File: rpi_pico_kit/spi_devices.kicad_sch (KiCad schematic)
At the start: 32 parts, among them J6 Conn_01x08_Male, J7 Conn_01x08_Male, J8 Conn_01x08_Male, J9 Micro_SD_Card_Det, SW10 SW_Push, SW7 SW_Push, SW8 SW_Push, SW9 SW_Push, U7 MCP23S08-xSO

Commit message: changed switches from tht to smd
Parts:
- SW10, SW7, SW8, SW9: footprint Button_Switch_THT:SW_TH_Tactile_Omron_B3F-10xx -> Button_Switch_SMD:SW_SPST_Omron_B3FS-100xP; Manufacturer Part Number LA215000 -> TD-03XAT-A00-TR; Supplier Laskakit -> GME; Supplier Part URL https://www.laskakit.cz/tlacitko-6x6x5mm/ -> https://www.gme.cz/td-03xa-t-smd
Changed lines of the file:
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@@
       (effects (font (size 1.27 1.27)) (justify right))
     )
-    (property "Footprint" "Button_Switch_THT:SW_TH_Tactile_Omron_B3F-10xx" (id 2) (at 128.27 38.1 0)
+    (property "Footprint" "Button_Switch_SMD:SW_SPST_Omron_B3FS-100xP" (id 2) (at 128.27 38.1 0)
       (effects (font (size 1.27 1.27)) hide)
     )
@@
       (effects (font (size 1.27 1.27)) hide)
     )
-    (property "Manufacturer Part Number" "LA215000" (id 4) (at 133.35 38.1 0)
-      (effects (font (size 1.27 1.27)) hide)
-    )
-    (property "Supplier" "Laskakit" (id 5) (at 133.35 38.1 0)
-      (effects (font (size 1.27 1.27)) hide)
-    )
-    (property "Supplier Part URL" "https://www.laskakit.cz/tlacitko-6x6x5mm/" (id 6) (at 133.35 38.1 0)
+    (property "Manufacturer Part Number" "TD-03XAT-A00-TR" (id 4) (at 133.35 38.1 0)
+      (effects (font (size 1.27 1.27)) hide)
+    )
+    (property "Supplier" "GME" (id 5) (at 133.35 38.1 0)
+      (effects (font (size 1.27 1.27)) hide)
+    )
+    (property "Supplier Part URL" "https://www.gme.cz/td-03xa-t-smd" (id 6) (at 133.35 38.1 0)
       (effects (font (size 1.27 1.27)) hide)
     )
@@
       (effects (font (size 1.27 1.27)) (justify right))
     )
-    (property "Footprint" "Button_Switch_THT:SW_TH_Tactile_Omron_B3F-10xx" (id 2) (at 166.37 38.1 0)
+    (property "Footprint" "Button_Switch_SMD:SW_SPST_Omron_B3FS-100xP" (id 2) (at 166.37 38.1 0)
       (effects (font (size 1.27 1.27)) hide)
     )
@@
       (effects (font (size 1.27 1.27)) hide)
     )
-    (property "Manufacturer Part Number" "LA215000" (id 4) (at 171.45 38.1 0)
-      (effects (font (size 1.27 1.27)) hide)
-    )
-    (property "Supplier" "Laskakit" (id 5) (at 171.45 38.1 0)
-      (effects (font (size 1.27 1.27)) hide)
-    )
-    (property "Supplier Part URL" "https://www.laskakit.cz/tlacitko-6x6x5mm/" (id 6) (at 171.45 38.1 0)
+    (property "Manufacturer Part Number" "TD-03XAT-A00-TR" (id 4) (at 171.45 38.1 0)
+      (effects (font (size 1.27 1.27)) hide)
+    )
+    (property "Supplier" "GME" (id 5) (at 171.45 38.1 0)
+      (effects (font (size 1.27 1.27)) hide)
+    )
+    (property "Supplier Part URL" "https://www.gme.cz/td-03xa-t-smd" (id 6) (at 171.45 38.1 0)
       (effects (font (size 1.27 1.27)) hide)
     )
@@
       (effects (font (size 1.27 1.27)) (justify right))
     )
-    (property "Footprint" "Button_Switch_THT:SW_TH_Tactile_Omron_B3F-10xx" (id 2) (at 140.97 38.1 0)
+    (property "Footprint" "Button_Switch_SMD:SW_SPST_Omron_B3FS-100xP" (id 2) (at 140.97 38.1 0)
       (effects (font (size 1.27 1.27)) hide)
     )
@@
       (effects (font (size 1.27 1.27)) hide)
     )
-    (property "Manufacturer Part Number" "LA215000" (id 4) (at 146.05 38.1 0)
-      (effects (font (size 1.27 1.27)) hide)
-    )
-    (property "Supplier" "Laskakit" (id 5) (at 146.05 38.1 0)
-      (effects (font (size 1.27 1.27)) hide)
-    )
-    (property "Supplier Part URL" "https://www.laskakit.cz/tlacitko-6x6x5mm/" (id 6) (at 146.05 38.1 0)
+    (property "Manufacturer Part Number" "TD-03XAT-A00-TR" (id 4) (at 146.05 38.1 0)
+      (effects (font (size 1.27 1.27)) hide)
+    )
+    (property "Supplier" "GME" (id 5) (at 146.05 38.1 0)
+      (effects (font (size 1.27 1.27)) hide)
+    )
+    (property "Supplier Part URL" "https://www.gme.cz/td-03xa-t-smd" (id 6) (at 146.05 38.1 0)
       (effects (font (size 1.27 1.27)) hide)
     )
@@
       (effects (font (size 1.27 1.27)) (justify right))
     )
-    (property "Footprint" "Button_Switch_THT:SW_TH_Tactile_Omron_B3F-10xx" (id 2) (at 153.67 38.1 0)
+    (property "Footprint" "Button_Switch_SMD:SW_SPST_Omron_B3FS-100xP" (id 2) (at 153.67 38.1 0)
       (effects (font (size 1.27 1.27)) hide)
     )
@@
       (effects (font (size 1.27 1.27)) hide)
     )
-    (property "Manufacturer Part Number" "LA215000" (id 4) (at 158.75 38.1 0)
-      (effects (font (size 1.27 1.27)) hide)
-    )
-    (property "Supplier" "Laskakit" (id 5) (at 158.75 38.1 0)
-      (effects (font (size 1.27 1.27)) hide)
-    )
-    (property "Supplier Part URL" "https://www.laskakit.cz/tlacitko-6x6x5mm/" (id 6) (at 158.75 38.1 0)
-      (effects (font (size 1.27 1.27)) hide)
-    )
+    (property "Manufacturer Part Number" "TD-03XAT-A00-TR" (id 4) (at 158.75 38.1 0)
+      (effects (font (size 1.27 1.27)) hide)
+    )
+    (property "Supplier" "GME" (id 5) (at 158.75 38.1 0)
+      (effects (font (size 1.27 1.27)) hide)
+    )
+    (property "Supplier Part URL" "https://www.gme.cz/td-03xa-t-smd" (id 6) (at 158.75 38.1 0)
+      (effects (font (size 1.27 1.27)) hide)
+    )

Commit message: changed footprint for tactile switches, added 3D model
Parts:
- SW10, SW7, SW8, SW9: footprint Button_Switch_SMD:SW_SPST_Omron_B3FS-100xP -> Button_Switch_SMD:SW_SPST_Omron_B3FS-100xP_12
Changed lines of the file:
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@@
       (effects (font (size 1.27 1.27)) (justify right))
     )
-    (property "Footprint" "Button_Switch_SMD:SW_SPST_Omron_B3FS-100xP" (id 2) (at 128.27 38.1 0)
+    (property "Footprint" "Button_Switch_SMD:SW_SPST_Omron_B3FS-100xP_12" (id 2) (at 128.27 38.1 0)
       (effects (font (size 1.27 1.27)) hide)
     )
@@
       (effects (font (size 1.27 1.27)) (justify right))
     )
-    (property "Footprint" "Button_Switch_SMD:SW_SPST_Omron_B3FS-100xP" (id 2) (at 166.37 38.1 0)
+    (property "Footprint" "Button_Switch_SMD:SW_SPST_Omron_B3FS-100xP_12" (id 2) (at 166.37 38.1 0)
       (effects (font (size 1.27 1.27)) hide)
     )
@@
       (effects (font (size 1.27 1.27)) (justify right))
     )
-    (property "Footprint" "Button_Switch_SMD:SW_SPST_Omron_B3FS-100xP" (id 2) (at 140.97 38.1 0)
+    (property "Footprint" "Button_Switch_SMD:SW_SPST_Omron_B3FS-100xP_12" (id 2) (at 140.97 38.1 0)
       (effects (font (size 1.27 1.27)) hide)
     )
@@
       (effects (font (size 1.27 1.27)) (justify right))
     )
-    (property "Footprint" "Button_Switch_SMD:SW_SPST_Omron_B3FS-100xP" (id 2) (at 153.67 38.1 0)
-      (effects (font (size 1.27 1.27)) hide)
-    )
+    (property "Footprint" "Button_Switch_SMD:SW_SPST_Omron_B3FS-100xP_12" (id 2) (at 153.67 38.1 0)
+      (effects (font (size 1.27 1.27)) hide)
+    )

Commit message: created Custom library with custom SMD button switch
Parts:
- SW10, SW7, SW8, SW9: footprint Button_Switch_SMD:SW_SPST_Omron_B3FS-100xP_12 -> Custom:SW_SPST_Omron_B3FS-100xP_12
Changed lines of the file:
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@@
       (effects (font (size 1.27 1.27)) (justify right))
     )
-    (property "Footprint" "Button_Switch_SMD:SW_SPST_Omron_B3FS-100xP_12" (id 2) (at 128.27 38.1 0)
+    (property "Footprint" "Custom:SW_SPST_Omron_B3FS-100xP_12" (id 2) (at 128.27 38.1 0)
       (effects (font (size 1.27 1.27)) hide)
     )
@@
       (effects (font (size 1.27 1.27)) (justify right))
     )
-    (property "Footprint" "Button_Switch_SMD:SW_SPST_Omron_B3FS-100xP_12" (id 2) (at 166.37 38.1 0)
+    (property "Footprint" "Custom:SW_SPST_Omron_B3FS-100xP_12" (id 2) (at 166.37 38.1 0)
       (effects (font (size 1.27 1.27)) hide)
     )
@@
       (effects (font (size 1.27 1.27)) (justify right))
     )
-    (property "Footprint" "Button_Switch_SMD:SW_SPST_Omron_B3FS-100xP_12" (id 2) (at 140.97 38.1 0)
+    (property "Footprint" "Custom:SW_SPST_Omron_B3FS-100xP_12" (id 2) (at 140.97 38.1 0)
       (effects (font (size 1.27 1.27)) hide)
     )
@@
       (effects (font (size 1.27 1.27)) (justify right))
     )
-    (property "Footprint" "Button_Switch_SMD:SW_SPST_Omron_B3FS-100xP_12" (id 2) (at 153.67 38.1 0)
-      (effects (font (size 1.27 1.27)) hide)
-    )
+    (property "Footprint" "Custom:SW_SPST_Omron_B3FS-100xP_12" (id 2) (at 153.67 38.1 0)
+      (effects (font (size 1.27 1.27)) hide)
+    )

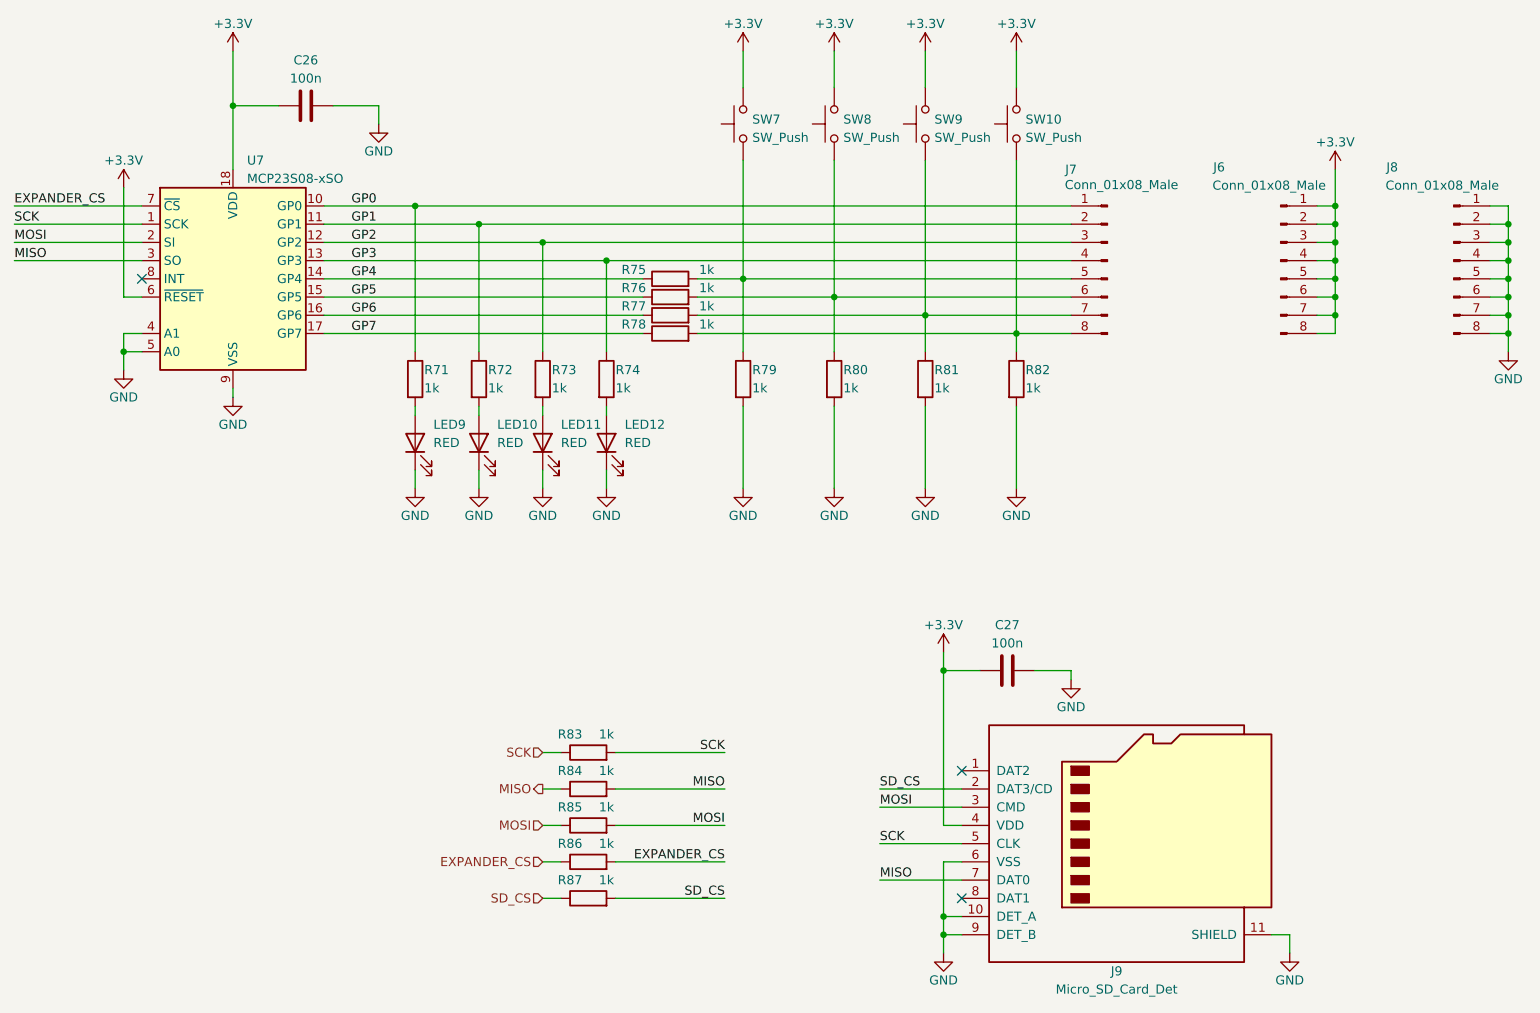
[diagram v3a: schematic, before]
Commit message: changed resistors to resistor arrays
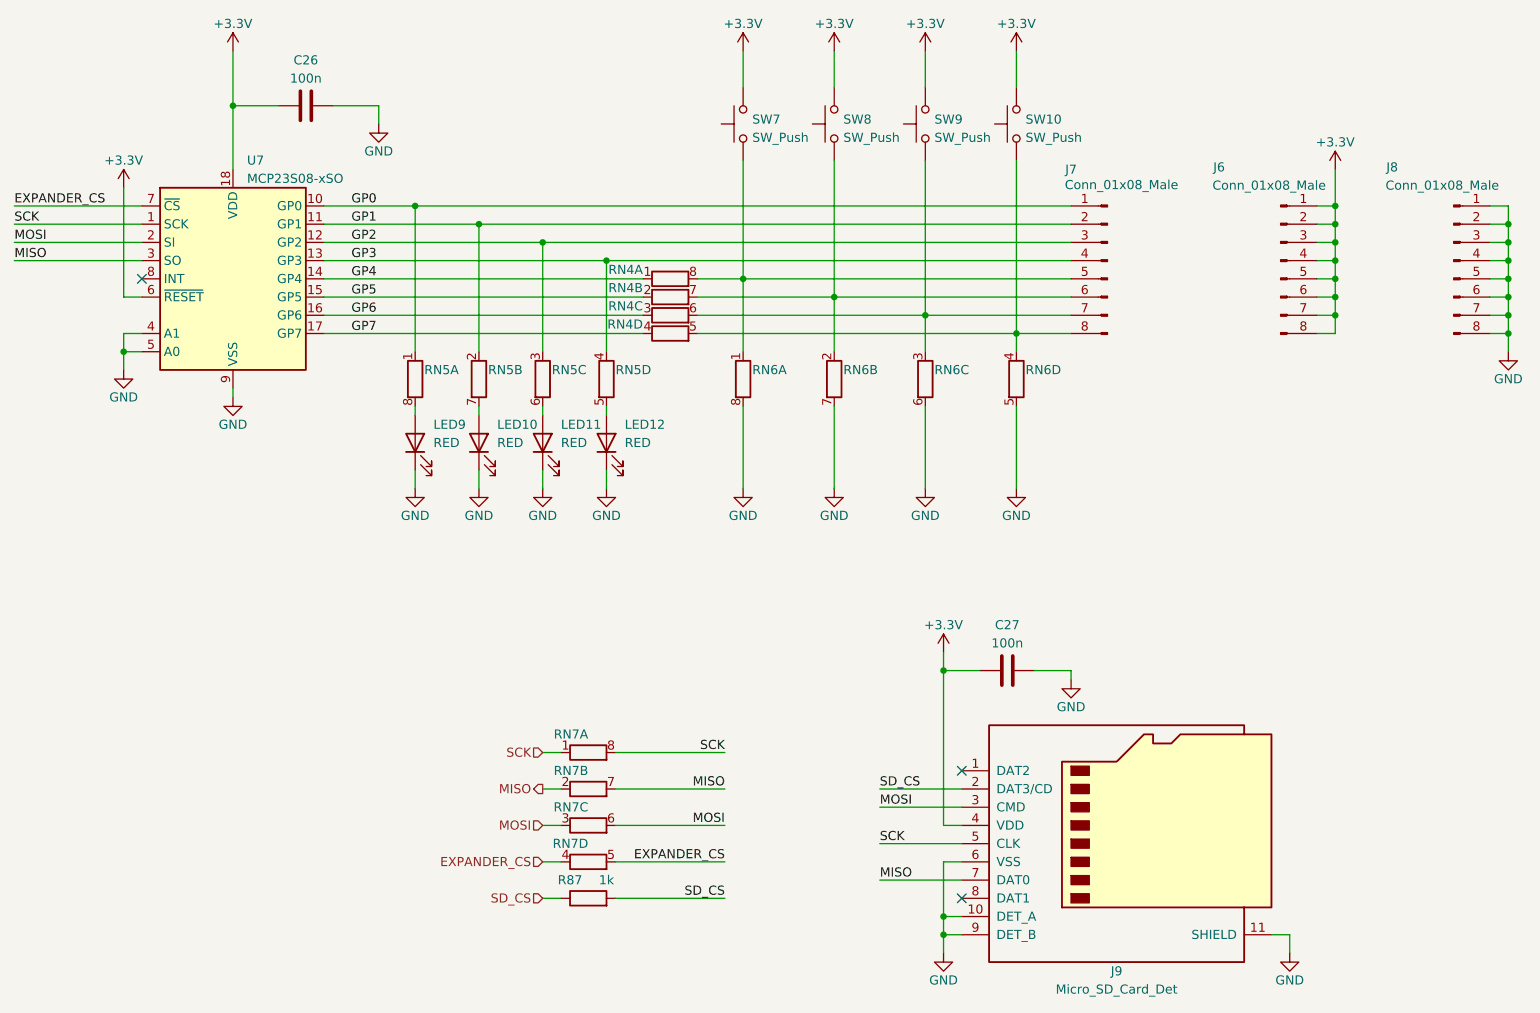
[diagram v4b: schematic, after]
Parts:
- removed R71, R72, R73, R74, R75, R76, R77, R78, R79, R80, R81, R82, R83, R84, R85, R86: 1k, Resistor_SMD:R_0805_2012Metric_Pad1.20x1.40mm_HandSolder, symbol Device:R
- added RN4, RN5, RN6, RN7: (no value), symbol Device:R_Pack04_Split
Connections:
- net EXPANDER_CS: now also RN7.4 (R4.1), RN7.5 (R4.2)
- net GND: now also RN6.5 (R4.2), RN6.6 (R3.2), RN6.7 (R2.2), RN6.8 (R1.2)
- net GP0: now also RN5.1 (R1.1)
- net GP1: now also RN5.2 (R2.1)
- net GP2: now also RN5.3 (R3.1)
- net GP3: now also RN5.4 (R4.1)
- net GP4: now also RN4.1 (R1.1)
- net GP5: now also RN4.2 (R2.1)
- net GP6: now also RN4.3 (R3.1)
- net GP7: now also RN4.4 (R4.1)
- net MISO: now also RN7.2 (R2.1), RN7.7 (R2.2)
- net MOSI: now also RN7.3 (R3.1), RN7.6 (R3.2)
- net SCK: now also RN7.1 (R1.1), RN7.8 (R1.2)
- net at LED10.2 (A): now also RN5.7 (R2.2)
- net at J7.6 (Pin_6), SW8.1: now also RN4.7 (R2.2), RN6.2 (R2.1)
- net at LED12.2 (A): now also RN5.5 (R4.2)
- net at J7.8 (Pin_8), SW10.1: now also RN4.5 (R4.2), RN6.4 (R4.1)
- net at J7.5 (Pin_5), SW7.1: now also RN4.8 (R1.2), RN6.1 (R1.1)
- net at J7.7 (Pin_7), SW9.1: now also RN4.6 (R3.2), RN6.3 (R3.1)
- net at LED9.2 (A): now also RN5.8 (R1.2)
- net at LED11.2 (A): now also RN5.6 (R3.2)

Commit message: added footprints for resistor arrays
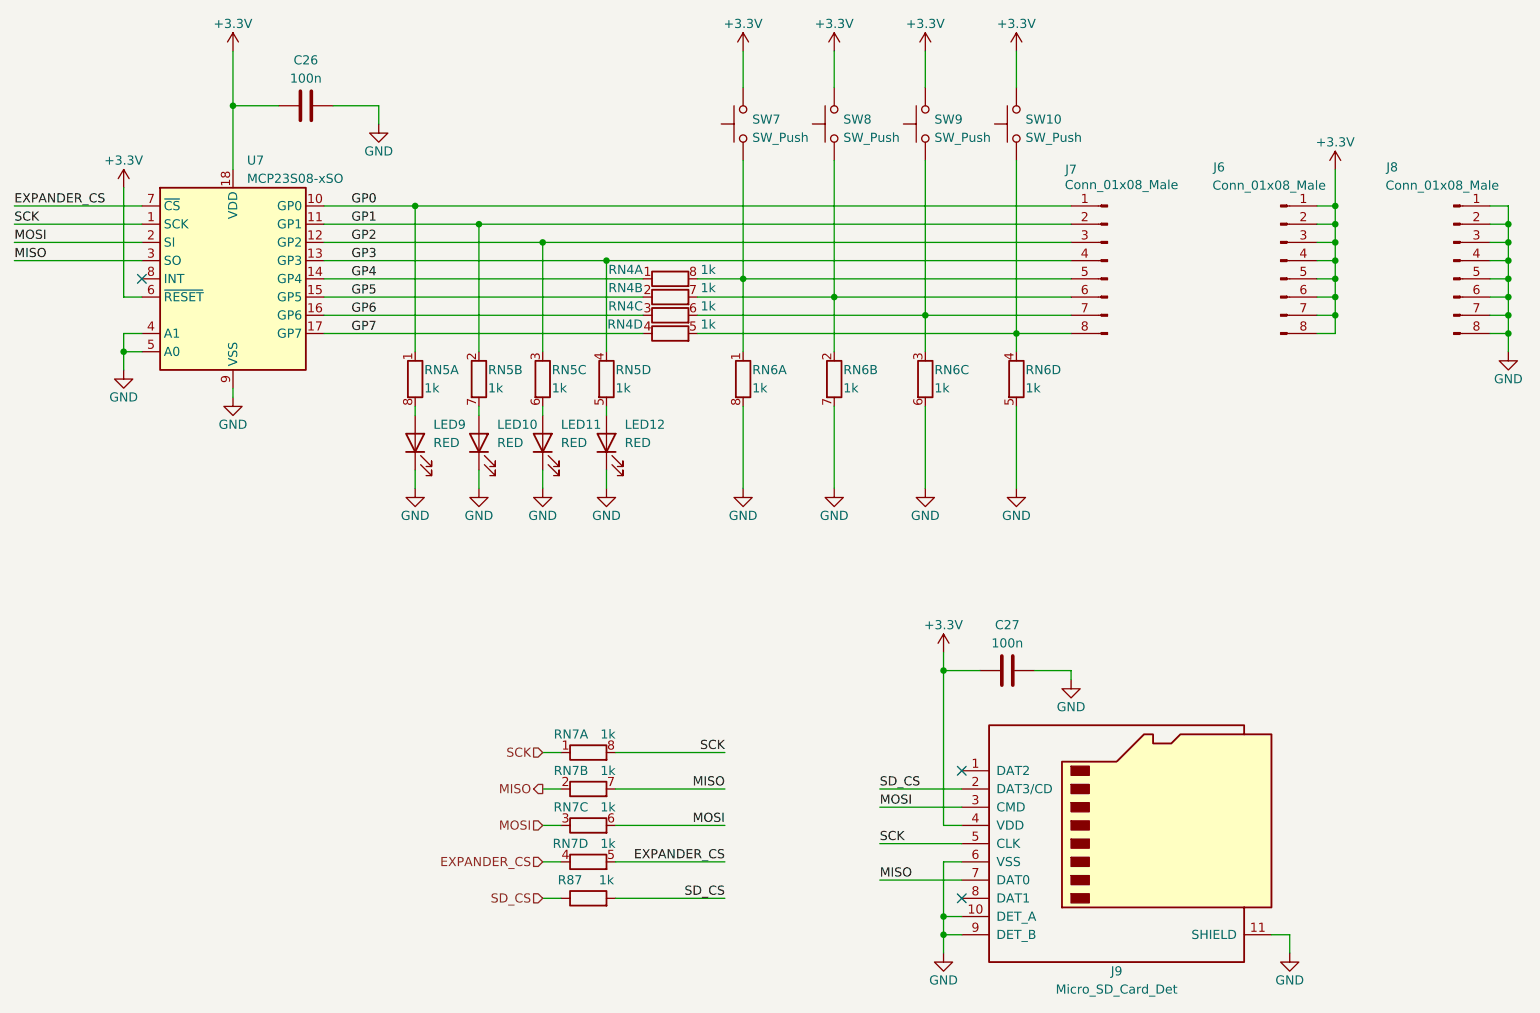
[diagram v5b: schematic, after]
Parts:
- RN4, RN5, RN6, RN7: value (none) -> 1k
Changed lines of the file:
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@@
       (effects (font (size 1.27 1.27)) (justify right))
     )
-    (property "Value" "" (id 1) (at 115.57 74.93 0)
+    (property "Value" "1k" (id 1) (at 115.57 74.93 0)
       (effects (font (size 1.27 1.27)) (justify right))
     )
@@
       (effects (font (size 1.27 1.27)) (justify right))
     )
-    (property "Value" "" (id 1) (at 129.54 58.42 90)
+    (property "Value" "1k" (id 1) (at 129.54 58.42 90)
       (effects (font (size 1.27 1.27)) (justify right))
     )
@@
       (effects (font (size 1.27 1.27)) (justify right))
     )
-    (property "Value" "" (id 1) (at 134.62 74.93 0)
+    (property "Value" "1k" (id 1) (at 134.62 74.93 0)
       (effects (font (size 1.27 1.27)) (justify right))
     )
@@
       (effects (font (size 1.27 1.27)) (justify right))
     )
-    (property "Value" "" (id 1) (at 88.9 74.93 0)
+    (property "Value" "1k" (id 1) (at 88.9 74.93 0)
       (effects (font (size 1.27 1.27)) (justify right))
     )
@@
       (effects (font (size 1.27 1.27)) (justify right))
     )
-    (property "Value" "" (id 1) (at 115.57 123.19 90)
+    (property "Value" "1k" (id 1) (at 115.57 123.19 90)
       (effects (font (size 1.27 1.27)) (justify right))
     )
@@
       (effects (font (size 1.27 1.27)) (justify right))
     )
-    (property "Value" "" (id 1) (at 129.54 63.5 90)
+    (property "Value" "1k" (id 1) (at 129.54 63.5 90)
       (effects (font (size 1.27 1.27)) (justify right))
     )
@@
       (effects (font (size 1.27 1.27)) (justify right))
     )
-    (property "Value" "" (id 1) (at 115.57 128.27 90)
+    (property "Value" "1k" (id 1) (at 115.57 128.27 90)
       (effects (font (size 1.27 1.27)) (justify right))
     )
@@
       (effects (font (size 1.27 1.27)) (justify right))
     )
-    (property "Value" "" (id 1) (at 172.72 74.93 0)
+    (property "Value" "1k" (id 1) (at 172.72 74.93 0)
       (effects (font (size 1.27 1.27)) (justify right))
     )
@@
       (effects (font (size 1.27 1.27)) (justify right))
     )
-    (property "Value" "" (id 1) (at 129.54 60.96 90)
+    (property "Value" "1k" (id 1) (at 129.54 60.96 90)
       (effects (font (size 1.27 1.27)) (justify right))
     )
@@
       (effects (font (size 1.27 1.27)) (justify right))
     )
-    (property "Value" "" (id 1) (at 115.57 138.43 90)
+    (property "Value" "1k" (id 1) (at 115.57 138.43 90)
       (effects (font (size 1.27 1.27)) (justify right))
     )
@@
       (effects (font (size 1.27 1.27)) (justify right))
     )
-    (property "Value" "" (id 1) (at 147.32 74.93 0)
+    (property "Value" "1k" (id 1) (at 147.32 74.93 0)
       (effects (font (size 1.27 1.27)) (justify right))
     )
@@
       (effects (font (size 1.27 1.27)) (justify right))
     )
-    (property "Value" "" (id 1) (at 97.79 74.93 0)
+    (property "Value" "1k" (id 1) (at 97.79 74.93 0)
       (effects (font (size 1.27 1.27)) (justify right))
     )
@@
       (effects (font (size 1.27 1.27)) (justify right))
     )
-    (property "Value" "" (id 1) (at 106.68 74.93 0)
+    (property "Value" "1k" (id 1) (at 106.68 74.93 0)
       (effects (font (size 1.27 1.27)) (justify right))
     )
@@
       (effects (font (size 1.27 1.27)) (justify right))
     )
-    (property "Value" "" (id 1) (at 115.57 133.35 90)
+    (property "Value" "1k" (id 1) (at 115.57 133.35 90)
       (effects (font (size 1.27 1.27)) (justify right))
     )
@@
       (effects (font (size 1.27 1.27)) (justify right))
     )
-    (property "Value" "" (id 1) (at 129.54 66.04 90)
+    (property "Value" "1k" (id 1) (at 129.54 66.04 90)
       (effects (font (size 1.27 1.27)) (justify right))
     )
@@
       (effects (font (size 1.27 1.27)) (justify right))
     )
-    (property "Value" "" (id 1) (at 160.02 74.93 0)
-      (effects (font (size 1.27 1.27)) (justify right))
-    )
+    (property "Value" "1k" (id 1) (at 160.02 74.93 0)
+      (effects (font (size 1.27 1.27)) (justify right))
+    )
